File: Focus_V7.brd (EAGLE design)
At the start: 64.8 x 94 mm, 100 parts, among them X1 USB+SHIELD, Y1 16Mhz

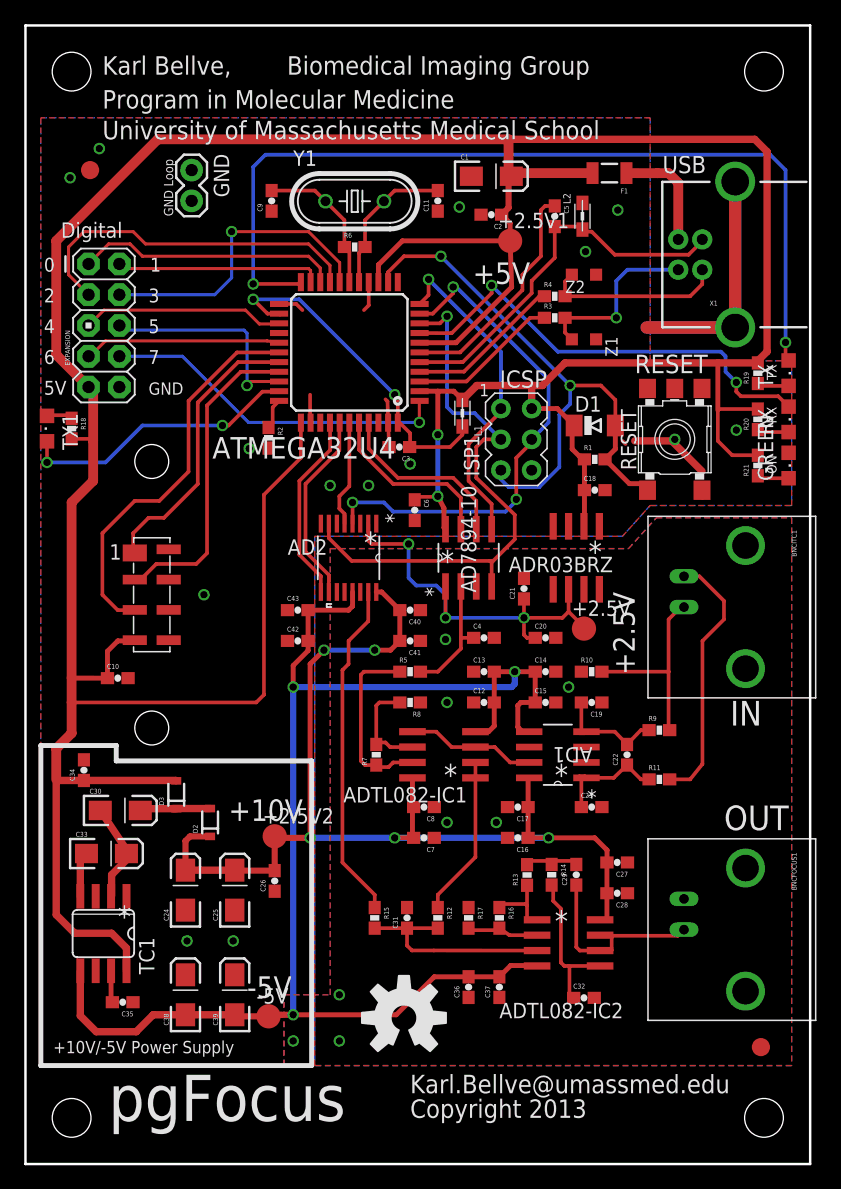
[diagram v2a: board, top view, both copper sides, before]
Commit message: LDAC pin of AD5531 needs to be tied to ground, Clean up of text
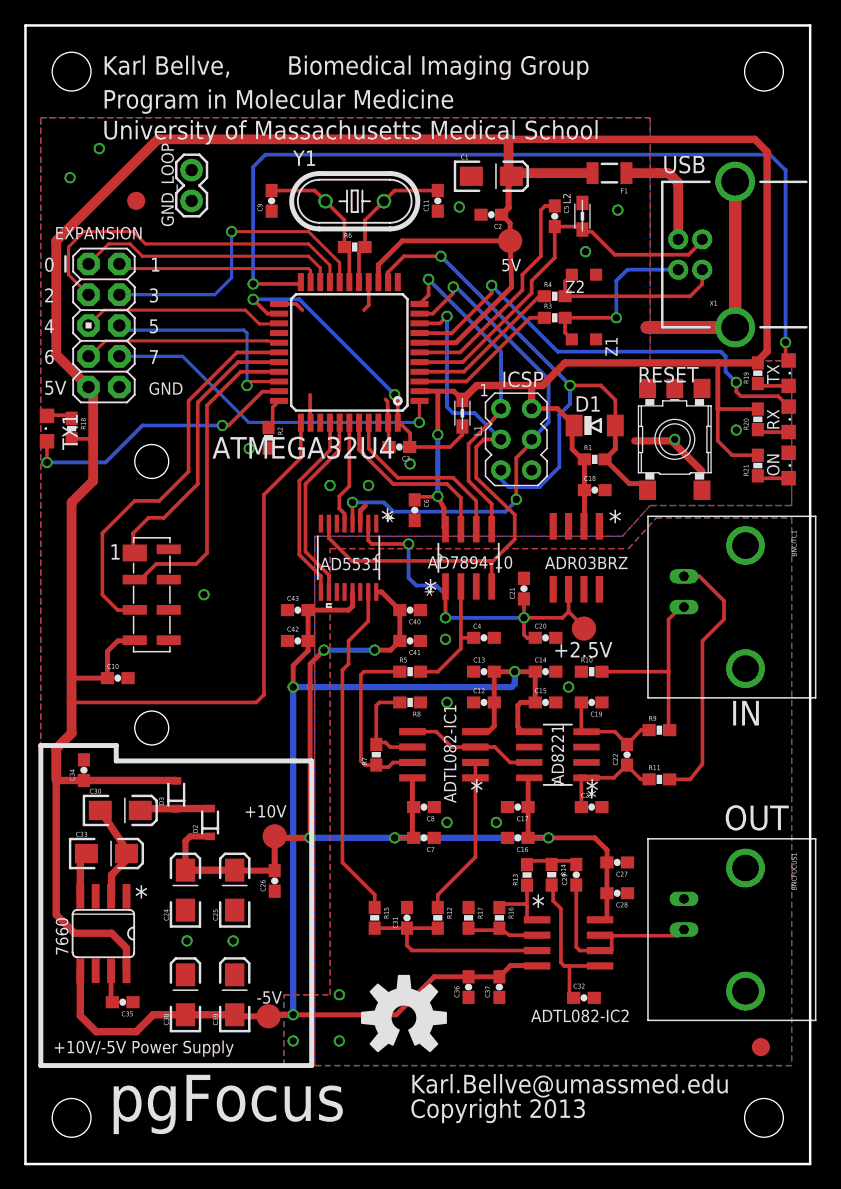
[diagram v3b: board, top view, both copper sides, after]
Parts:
- AD7894-10: value AD7894ARZ-3 -> AD7894ARZ-10
- D2, D3: value DIODE-SCHOTTKY_ -> NXP - 1PS76SB21,115
- F1: value PTCSMD -> MF-NSMF050-2
- L1, L2: value WE-CBF 0805 -> MH2029-300Y
- RESET: value SKHMPSE010 -> 688-SKHMQKE010
- moved JP2 4.58 mm to (44.7, 78.2)
- renumbered +2.5V1 to 5V, +2.5V2 to +10V, AD1 to AD8221, AD2 to AD5531, GND to GND_LOOP, GREEN to ON, ISP1 to ICSP, TC1 to 7660
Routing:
- net GND: track 57.1 -> 58.4 mm
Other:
- board text added: "Caps C24,C25,C38,C39 might not need to be low ESR"
- board text added: "Optional Cap (C35)"
- board text added: "slows the OSC (pin 7)"
- board text removed: "+10V"
- board text removed: "+2.5V"
- board text removed: "+5V"
- board text removed: "-5V"
- board text removed: "Digital"
- board text removed: "GND Loop"
- board text removed: "ICSP"
- board text removed: "ON"
- board text removed: "Optional Cap (C35) to"
- board text removed: "RESET"
- board text removed: "RX"
- board text removed: "TX"
- board text removed: "slow the OSC (pin 7)"
